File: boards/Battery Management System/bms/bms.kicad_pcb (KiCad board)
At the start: 2 copper layers, 50.8 x 101.6 mm, 25 parts, among them J1 Screw_Terminal_01x05, J2 1986660-2, J3 1986660-2, K1 HE1AN-W-DC6V-Y6, U1 BD48L32G, U2 BD48L32G, U3 BD48L32G, U4 BD48L32G, U5 SN74HC08DR, U6 TL071HIDBVR

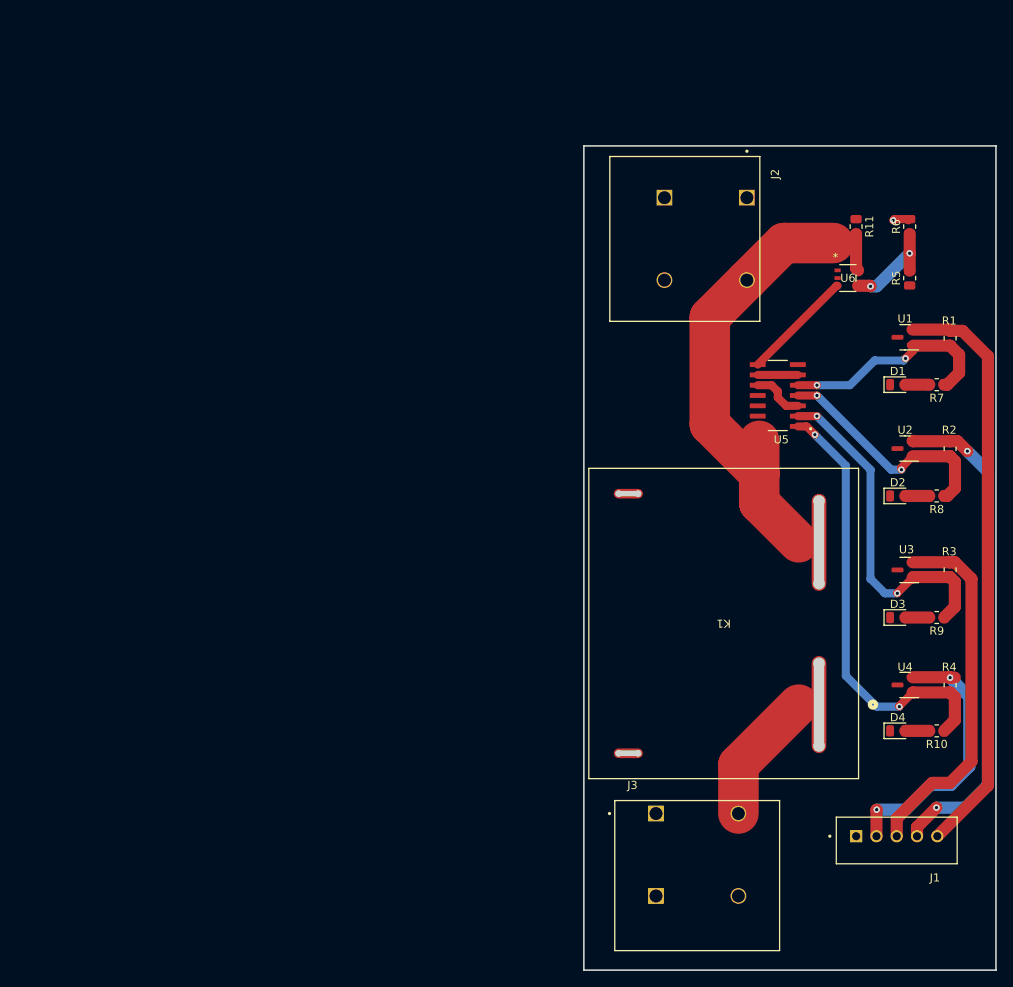
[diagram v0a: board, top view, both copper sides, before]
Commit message: Reduce board size
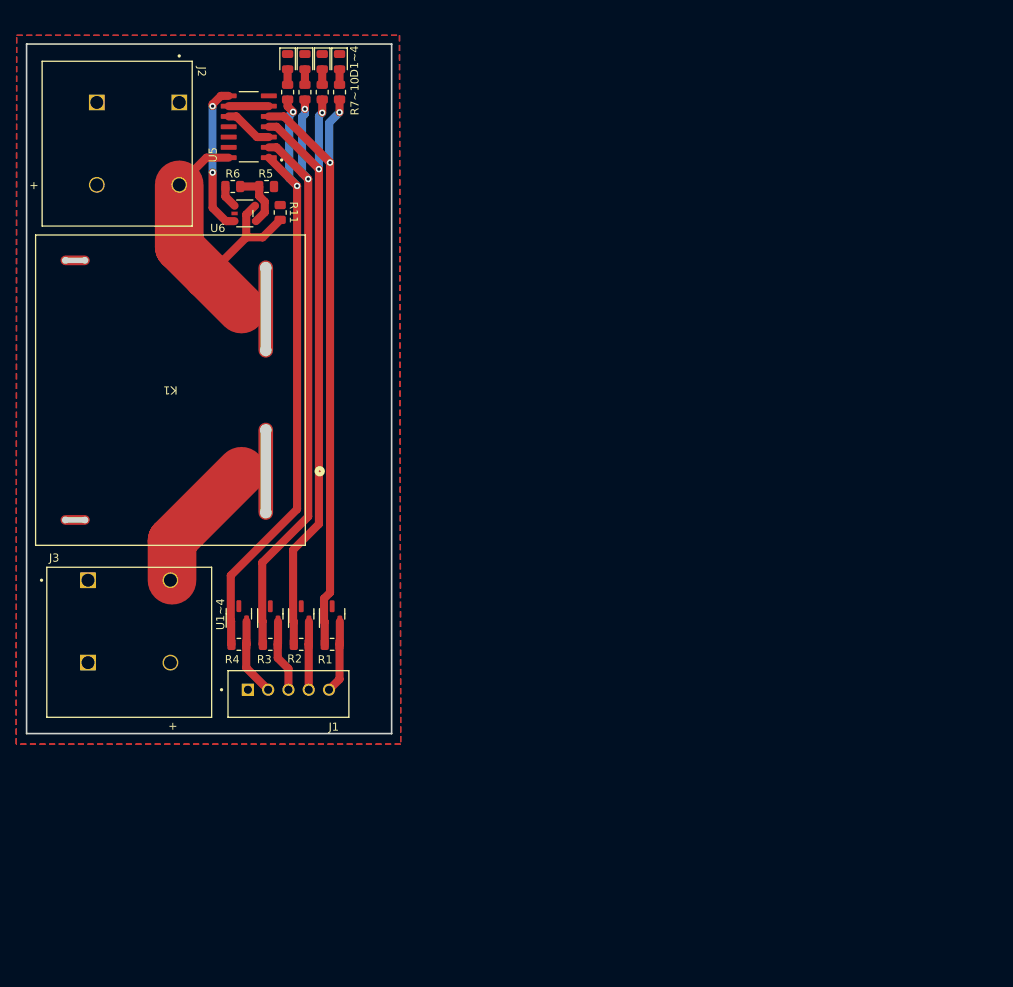
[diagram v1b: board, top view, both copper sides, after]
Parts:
- moved R10 112.3 mm to (57.2, 30.9), turned to 90 degrees
- moved D4 111.6 mm to (57.2, 27.2), turned to -90 degrees
- moved R9 101.3 mm to (59.3, 30.9), turned to 90 degrees
- moved D3 100.2 mm to (59.3, 27.2), turned to -90 degrees
- moved R8 90.6 mm to (61.4, 30.9), turned to 90 degrees
- moved D2 88.9 mm to (61.4, 27.2), turned to -90 degrees
- moved R4 87.8 mm to (51.2, 99.0), turned to 0 degrees
- moved R1 85.0 mm to (62.7, 99.0), turned to 0 degrees
- moved R3 84.3 mm to (55.0, 99.0), turned to 0 degrees
- moved R6 83.6 mm to (50.4, 42.6), turned to 180 degrees
- moved R2 83.5 mm to (58.9, 99.0), turned to 0 degrees
- moved U4 82.6 mm to (51.2, 95.2), turned to 90 degrees
- moved R7~10 82.0 mm to (63.6, 30.9), turned to 90 degrees
- moved R5 80.1 mm to (54.6, 42.6), turned to 180 degrees
- moved D1~4 79.5 mm to (63.6, 27.2), turned to -90 degrees
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- renumbered D1 to D1~4, R7 to R7~10, U1 to U1~4
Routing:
- net /V_CELL_1: track 72.4 -> 8.97 mm
- net /V_CELL_2: track 61.5 -> 8.43 mm, vias 2 -> 0
- net /CON_1: track 27.4 -> 78.0 mm
- net /CON_2: track 29.3 -> 77.0 mm
- net /V_CELL_3: track 44.9 -> 8.98 mm
- net /CON_3: track 42.3 -> 76.5 mm
- net /V_CELL_4: track 34.1 -> 9.56 mm, vias 2 -> 0
- net /CON_4: track 54.5 -> 76.4 mm
- net /V_BAT_IN: track 61.8 -> 42.1 mm
- net Net-(U6-IN-): track 12.6 -> 7.34 mm, vias 2 -> 0
- net Net-(U5-3Y): track 13.9 -> 18.6 mm, vias 0 -> 2
- net Net-(D4-A): track 2.96 -> 1.91 mm
- net Net-(D3-A): track 2.96 -> 1.91 mm
- net Net-(D2-A): track 2.96 -> 1.91 mm
- net Net-(D1-A): track 2.96 -> 1.91 mm
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- added copper zone on B.Cu, net GND
- added copper zone on F.Cu, net GND
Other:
- board size 50.8 x 101.6 mm -> 45 x 85 mm
- board text added: "+"

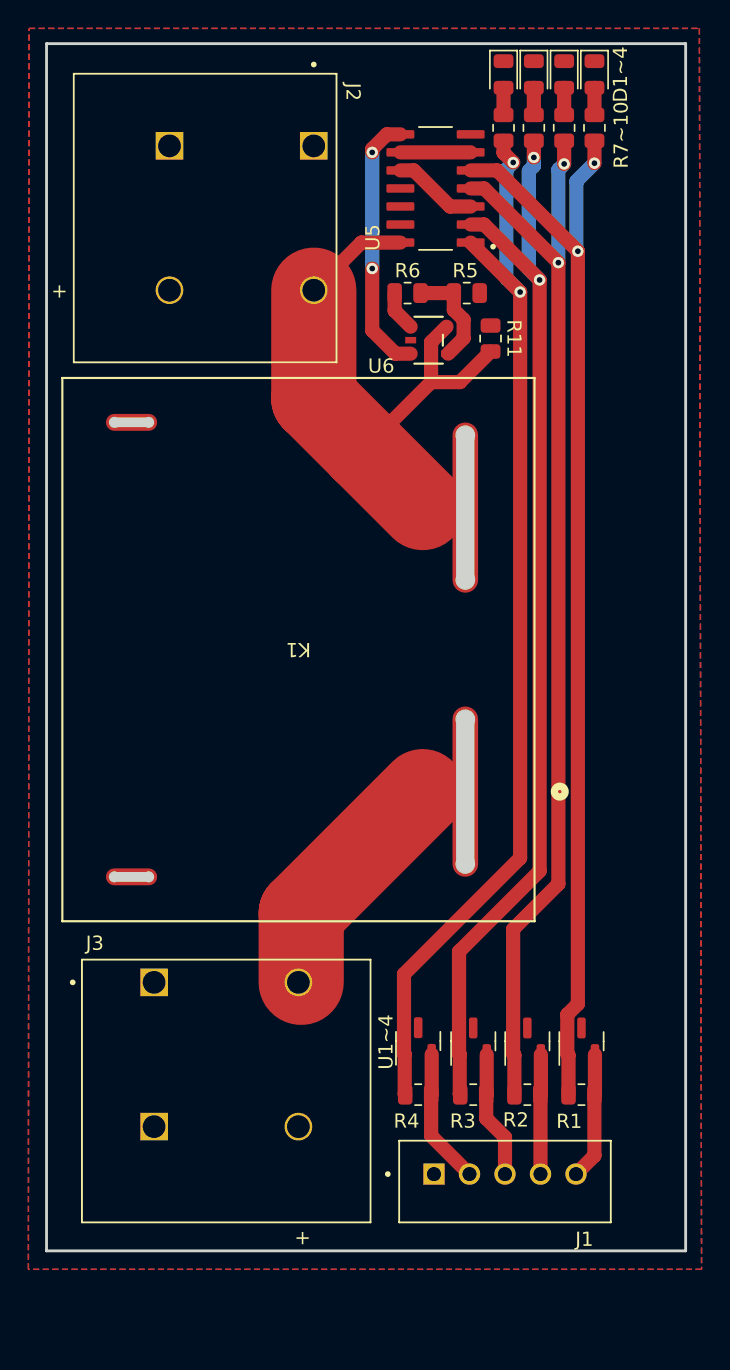
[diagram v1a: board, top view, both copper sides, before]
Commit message: Changed JST onnector
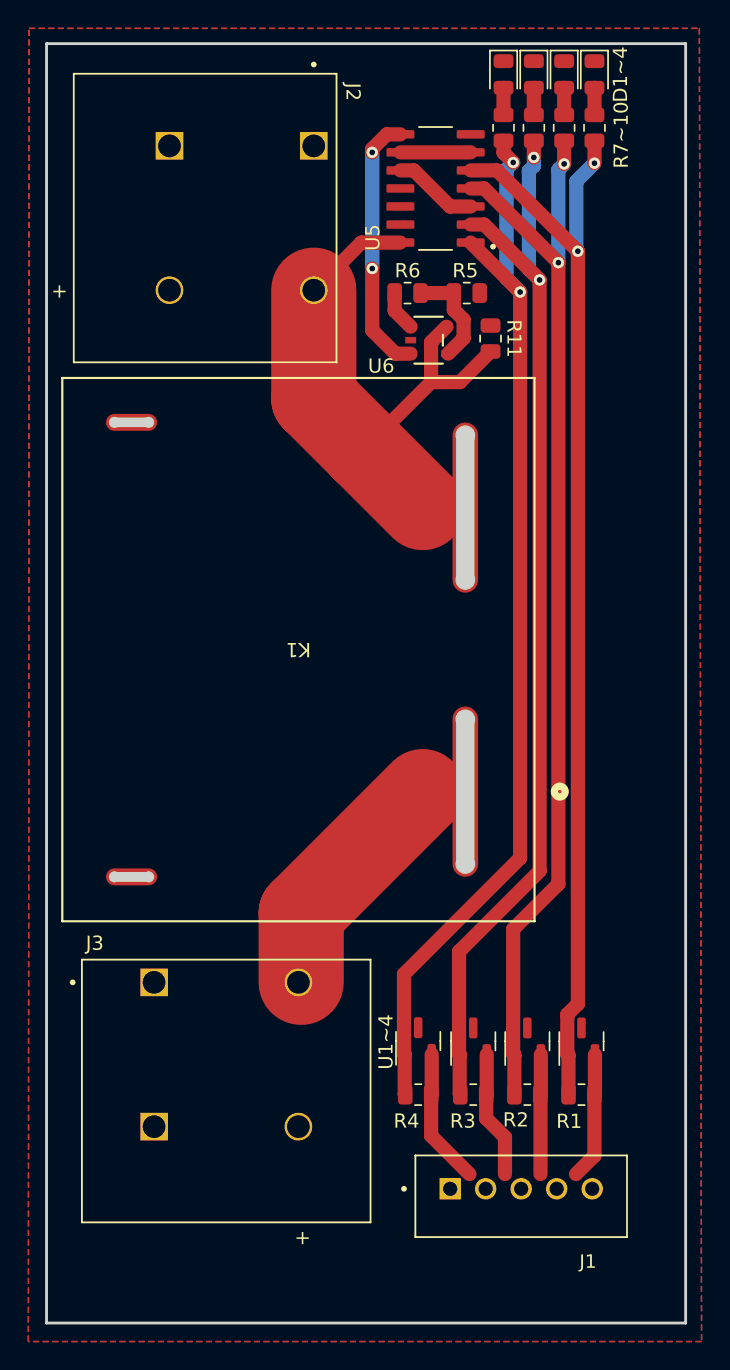
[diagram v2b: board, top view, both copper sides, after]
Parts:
- J1: value Screw_Terminal_01x05 -> JST 5-pin; footprint B5B_XH_A:JST_B5B-XH-A -> footprints:JST_B5B-XH-A
- moved J1 1.54 mm to (58.4, 106.2)
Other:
- board size 45 x 85 mm -> 45 x 90.1 mm

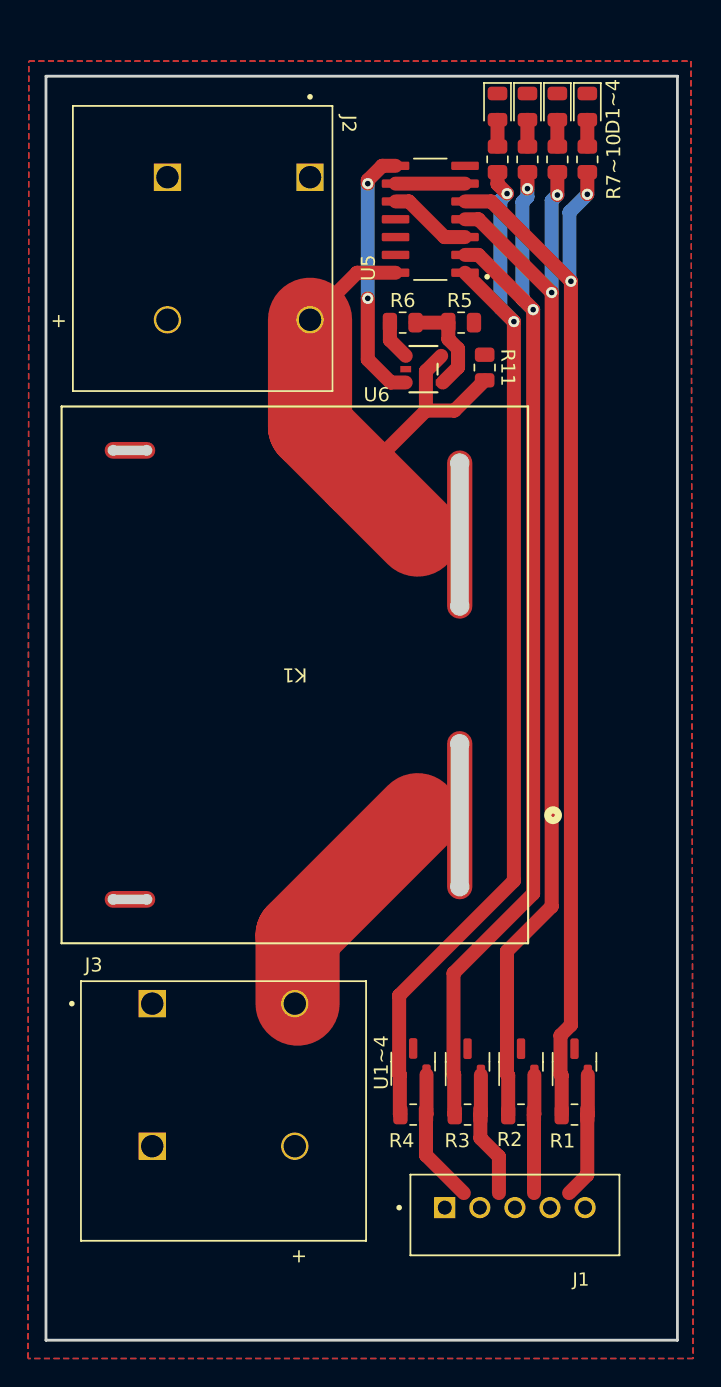
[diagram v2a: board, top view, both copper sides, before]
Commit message: BMS updated circuit
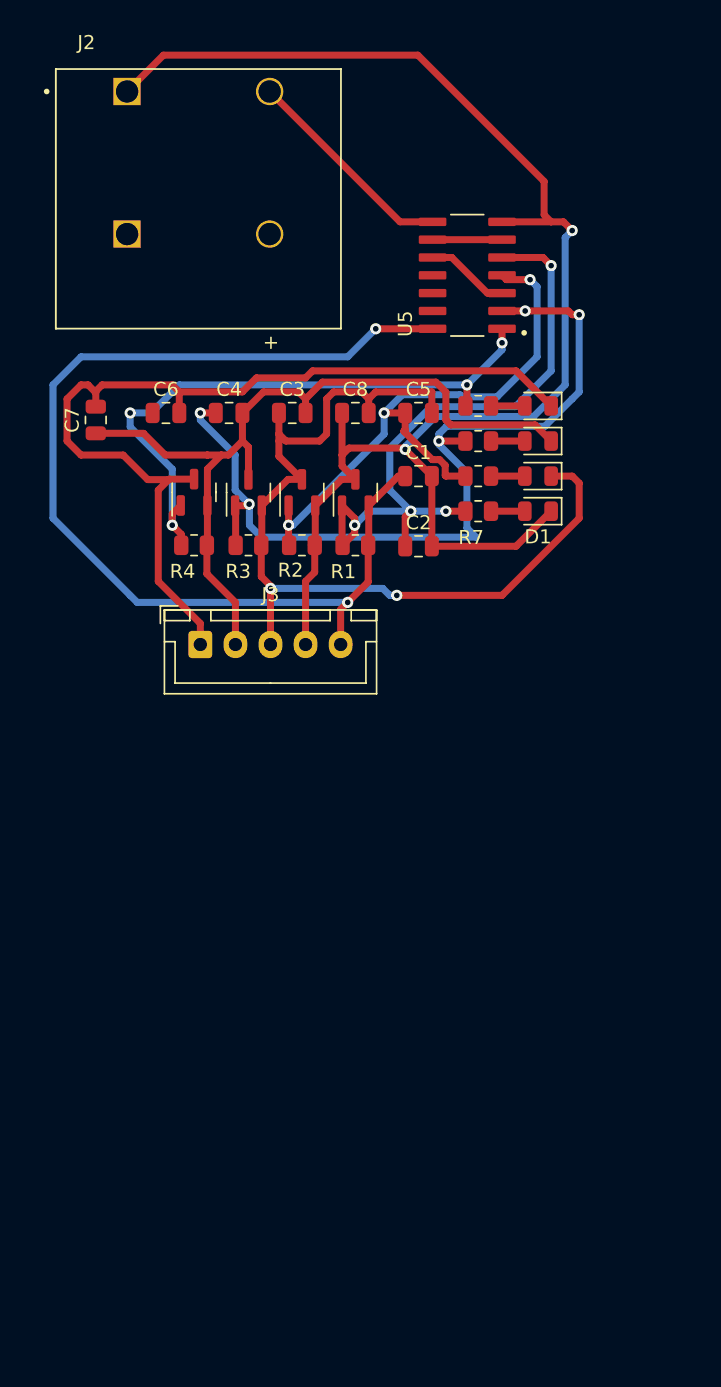
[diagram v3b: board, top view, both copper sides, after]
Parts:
- removed J1: JST 5-pin, footprints:JST_B5B-XH-A
- removed K1: HE1AN-W-DC6V-Y6, HE1AN_W_DC6V_Y6:HE1AN-W-DC6V_PAN
- removed R11: 100kΩ, Resistor_SMD:R_0805_2012Metric
- removed R5: 10kΩ, Resistor_SMD:R_0805_2012Metric
- removed R6: 5kΩ, Resistor_SMD:R_0805_2012Metric
- removed U6: TL071HIDBVR, TL071HIDBVR:SOT23_DBV_5_TEX-L
- added C1: 10uF, Capacitor_SMD:C_0805_2012Metric, F.Cu at (51.5, 53.5)
- added C2: 10uF, Capacitor_SMD:C_0805_2012Metric, F.Cu at (51.5, 58.5)
- added C3: 10uF, Capacitor_SMD:C_0805_2012Metric, F.Cu at (42.5, 49.0)
- added C4: 10uF, Capacitor_SMD:C_0805_2012Metric, F.Cu at (38.0, 49.0)
- added C5: 10uF, Capacitor_SMD:C_0805_2012Metric, F.Cu at (51.5, 49.0)
- added C6: 10uF, Capacitor_SMD:C_0805_2012Metric, F.Cu at (33.5, 49.0)
- added C7: 10uF, Capacitor_SMD:C_0805_2012Metric, F.Cu at (28.6, 49.5)
- added C8: 10uF, Capacitor_SMD:C_0805_2012Metric, F.Cu at (47.0, 49.0)
- J2: footprint 1986660_2a:TE_1986660-2 -> 1986660_2:TE_1986660-2
- J3: value 1986660-2 -> B5B-XH-A; footprint 1986660_2a:TE_1986660-2 -> Connector_JST:JST_XH_B5B-XH-A_1x05_P2.50mm_Vertical
- R1, R2, R3, R4: value 5MΩ -> 1MΩ
- moved U1 43.5 mm to (47.0, 54.7)
- moved U2 43.5 mm to (43.2, 54.7)
- moved U3 43.5 mm to (39.4, 54.7)
- moved R1 43.5 mm to (47.0, 58.4)
- moved R2 43.5 mm to (43.2, 58.4)
- moved R3 43.5 mm to (39.4, 58.4)
- moved R4 43.5 mm to (35.6, 58.4)
- moved U4 43.5 mm to (35.6, 54.7)
- moved D1 29.0 mm to (60.1, 56.0), turned to 180 degrees
- moved D2 26.4 mm to (60.1, 53.5), turned to 180 degrees
- moved R7 26.2 mm to (55.8, 56.0), turned to 0 degrees
- moved J3 25.8 mm to (36.0, 65.5)
- moved D3 23.8 mm to (60.1, 51.0), turned to 180 degrees
- moved R8 23.3 mm to (55.8, 53.5), turned to 0 degrees
- moved D4 21.5 mm to (60.1, 48.5), turned to 180 degrees
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- renumbered D1~4 to D1, R7~10 to R7, U1~4 to U1
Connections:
- D1 pad 1: GND -> /V_CELL_2
- D2 pad 1: GND -> /V_CELL_3
- D3 pad 1: GND -> /V_CELL_4
- J2 pad 1_1: GND -> /V_CELL_2
- J2 pad 2_1: /V_BAT_IN -> /V_OUT
- U1 pad 3: GND -> /V_CELL_2
- U2 pad 3: GND -> /V_CELL_3
- U3 pad 3: GND -> /V_CELL_4
- U5 pad 14: /V_BAT_IN -> /V_CELL_1
- U5 pad 7: GND -> /V_CELL_2
- U5 pad 8: Net-(U5-3Y) -> /V_OUT
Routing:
- net /V_CELL_2: track 8.43 -> 108.4 mm, vias 0 -> 2
- net /V_CELL_1: track 8.97 -> 75.9 mm, vias 0 -> 2
- net GND: track 0.00 -> 66.3 mm
- net /V_CELL_3: track 8.98 -> 65.4 mm, vias 0 -> 2
- net /V_CELL_4: track 9.56 -> 59.1 mm
- net /V_BAT_IN: track 42.1 -> 0.00 mm
- net /CON_2: track 77.0 -> 43.3 mm, vias 2 -> 3
- net /CON_4: track 76.4 -> 44.0 mm, vias 2 -> 4
- net /CON_1: track 78.0 -> 47.6 mm, vias 2 -> 4
- net Net-(U5-3Y): track 18.6 -> 0.00 mm, vias 2 -> 0
- net /V_BAT_OUT: track 17.0 -> 0.00 mm
- net /V_OUT: track 0.00 -> 15.5 mm
- net /CON_3: track 76.5 -> 63.7 mm, vias 2 -> 5
- net Net-(U6-IN-): track 7.34 -> 0.00 mm
- net Net-(U6-OUT): track 2.83 -> 0.00 mm
- removed copper zone on B.Cu, net GND
- removed copper zone on F.Cu, net GND
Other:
- board outline removed
